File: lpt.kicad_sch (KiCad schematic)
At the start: 28 parts, among them J4 DB25 FEMALE, K1 OJS-SH-124HMF, Q4 BC847, Q5 BC857, U3 LM358, U4 74HC245, U5 74HC245, U6 ACSL-6310, U7 ACSL-6310

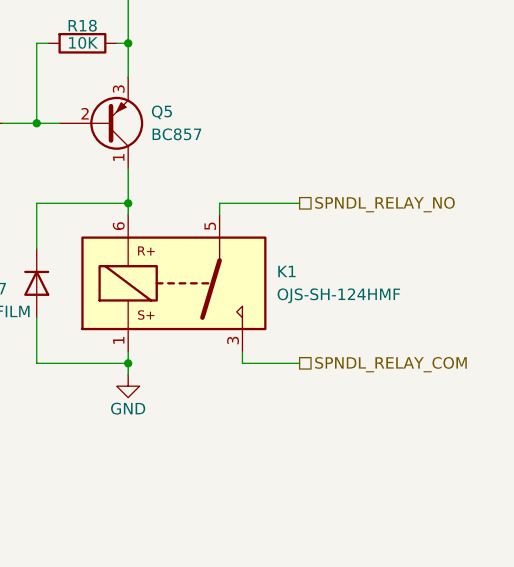
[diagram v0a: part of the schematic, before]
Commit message: Change and reposition JP16/17 connector to screw terminal.
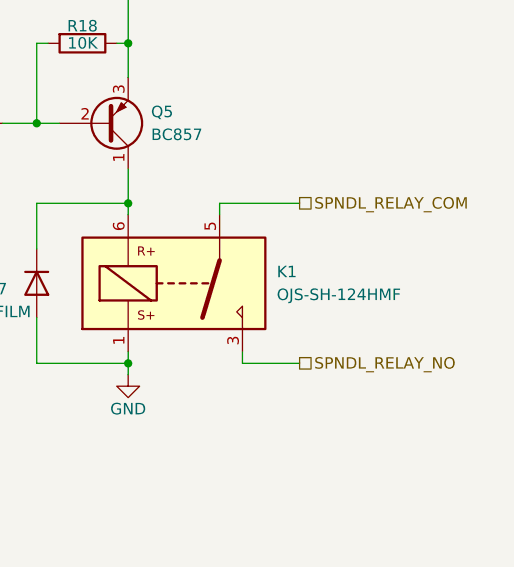
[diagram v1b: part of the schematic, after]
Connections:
- net SPNDL_RELAY_COM: now also K1.5; no longer K1.3
- net SPNDL_RELAY_NO: now also K1.3; no longer K1.5
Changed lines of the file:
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@@
     (effects (font (size 1.27 1.27)) (justify left))
   )
-  (hierarchical_label "SPNDL_RELAY_COM" (shape passive) (at 261.62 157.48 0)
+  (hierarchical_label "SPNDL_RELAY_COM" (shape passive) (at 261.62 139.7 0)
     (effects (font (size 1.27 1.27)) (justify left))
   )
@@
     (effects (font (size 1.27 1.27)) (justify left))
   )
-  (hierarchical_label "SPNDL_RELAY_NO" (shape passive) (at 261.62 139.7 0)
+  (hierarchical_label "SPNDL_RELAY_NO" (shape passive) (at 261.62 157.48 0)
     (effects (font (size 1.27 1.27)) (justify left))
   )
@@
       (effects (font (size 1.27 1.27)) hide)
     )
+    (pin "1")
+    (pin "2")
+    (pin "3")
     (pin "5")
     (pin "6")
     (pin "7")
+    (pin "4")
+    (pin "8")
   )
   (symbol (lib_id "Device:R_Pack04") (at 161.29 82.55 0) (mirror x) (unit 1)
@@
       (effects (font (size 1.27 1.27)) hide)
     )
+    (pin "1")
+    (pin "2")
+    (pin "3")
+    (pin "5")
+    (pin "6")
+    (pin "7")
     (pin "4")
     (pin "8")
@@
     (pin "2")
     (pin "3")
+    (pin "5")
+    (pin "6")
+    (pin "7")
+    (pin "4")
+    (pin "8")
   )
   (symbol (lib_id "Connector:DB25_Female_MountingHoles") (at 31.75 68.58 0) (mirror y) (unit 1)

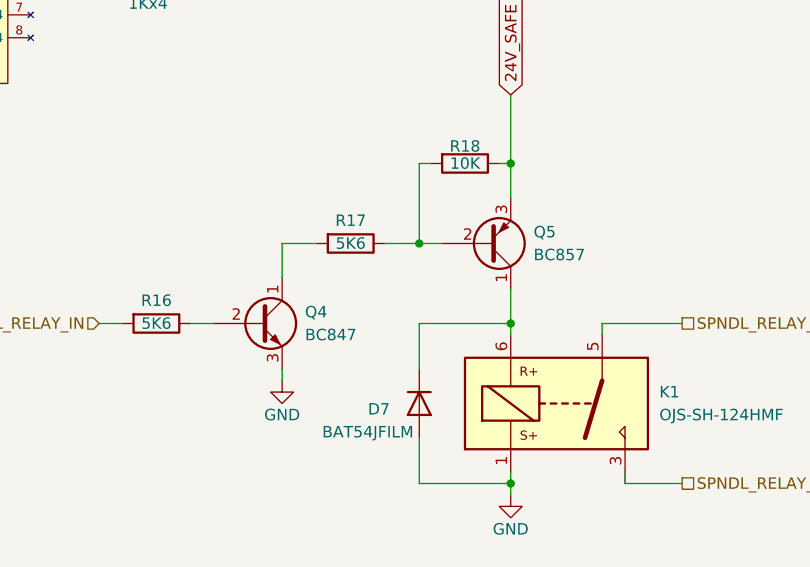
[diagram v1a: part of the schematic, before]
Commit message: Correct Q5 pin muddle.
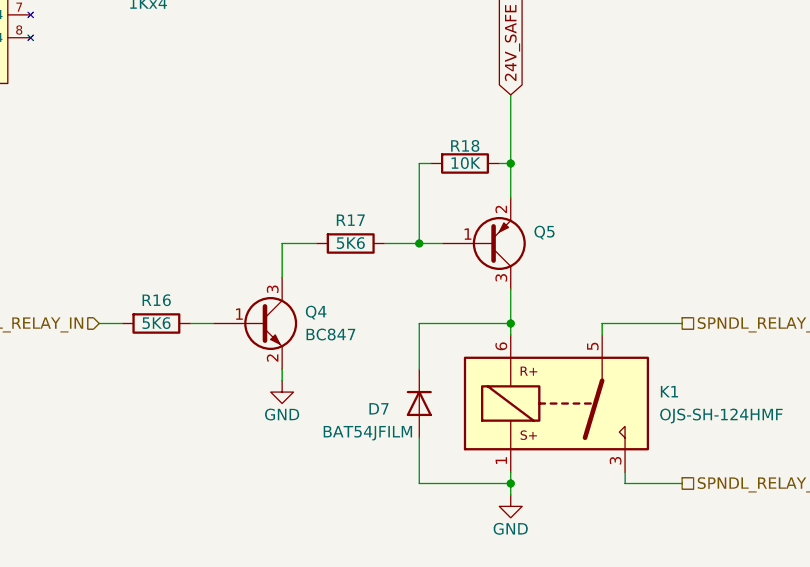
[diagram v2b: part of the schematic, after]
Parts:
- Q4: footprint -Project:SOT-23_DOT -> Package_TO_SOT_SMD:SOT-23; symbol Transistor_BJT:BC547 -> Transistor_BJT:BC847
- Q5: value BC857 -> (none); footprint -Project:SOT-23_DOT -> (none); symbol Device:Q_PNP_CBE -> Device:Q_PNP_BEC
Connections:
- net 24V_SAFE: now also Q5.2 (E); no longer Q5.3 (E)
- net GND: now also Q4.2 (E); no longer Q4.3 (E)
- net at D7.1 (K), K1.6: now also Q5.3 (C); no longer Q5.1 (C)
- net at R17.1, R18.2: now also Q5.1 (B); no longer Q5.2 (B)
- net at R16.1: now also Q4.1 (B); no longer Q4.2 (B)
- net at R17.2: now also Q4.3 (C); no longer Q4.1 (C)
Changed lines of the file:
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@@
     (pin "1")
   )
-  (symbol (lib_id "Device:Q_PNP_CBE") (at 240.03 130.81 0) (mirror x) (unit 1)
+  (symbol (lib_id "Device:Q_PNP_BEC") (at 240.03 130.81 0) (mirror x) (unit 1)
     (in_bom yes) (on_board yes) (fields_autoplaced)
     (property "Reference" "Q5" (id 0) (at 245.11 129.5399 0)
       (effects (font (size 1.27 1.27)) (justify left))
     )
-    (property "Value" "BC857" (id 1) (at 245.11 132.0799 0)
-      (effects (font (size 1.27 1.27)) (justify left))
-    )
-    (property "Footprint" "-Project:SOT-23_DOT" (id 2) (at 245.11 133.35 0)
+    (property "Value" "" (id 1) (at 245.11 132.0799 0)
+      (effects (font (size 1.27 1.27)) (justify left))
+    )
+    (property "Footprint" "" (id 2) (at 245.11 133.35 0)
       (effects (font (size 1.27 1.27)) hide)
     )
@@
     (pin "1")
   )
-  (symbol (lib_id "Transistor_BJT:BC547") (at 214.63 139.7 0) (unit 1)
+  (symbol (lib_id "Transistor_BJT:BC847") (at 214.63 139.7 0) (unit 1)
     (in_bom yes) (on_board yes)
     (property "Reference" "Q4" (id 0) (at 219.71 138.43 0)
@@
       (effects (font (size 1.27 1.27)) (justify left))
     )
-    (property "Footprint" "-Project:SOT-23_DOT" (id 2) (at 219.71 141.605 0)
+    (property "Footprint" "Package_TO_SOT_SMD:SOT-23" (id 2) (at 219.71 141.605 0)
       (effects (font (size 1.27 1.27) italic) (justify left) hide)
     )
-    (property "Datasheet" "https://www.onsemi.com/pub/Collateral/BC550-D.pdf" (id 3) (at 214.63 139.7 0)
+    (property "Datasheet" "http://www.infineon.com/dgdl/Infineon-BC847SERIES_BC848SERIES_BC849SERIES_BC850SERIES-DS-v01_01-en.pdf?fileId=db3a304314dca389011541d4630a1657" (id 3) (at 214.63 139.7 0)
       (effects (font (size 1.27 1.27)) (justify left) hide)
     )

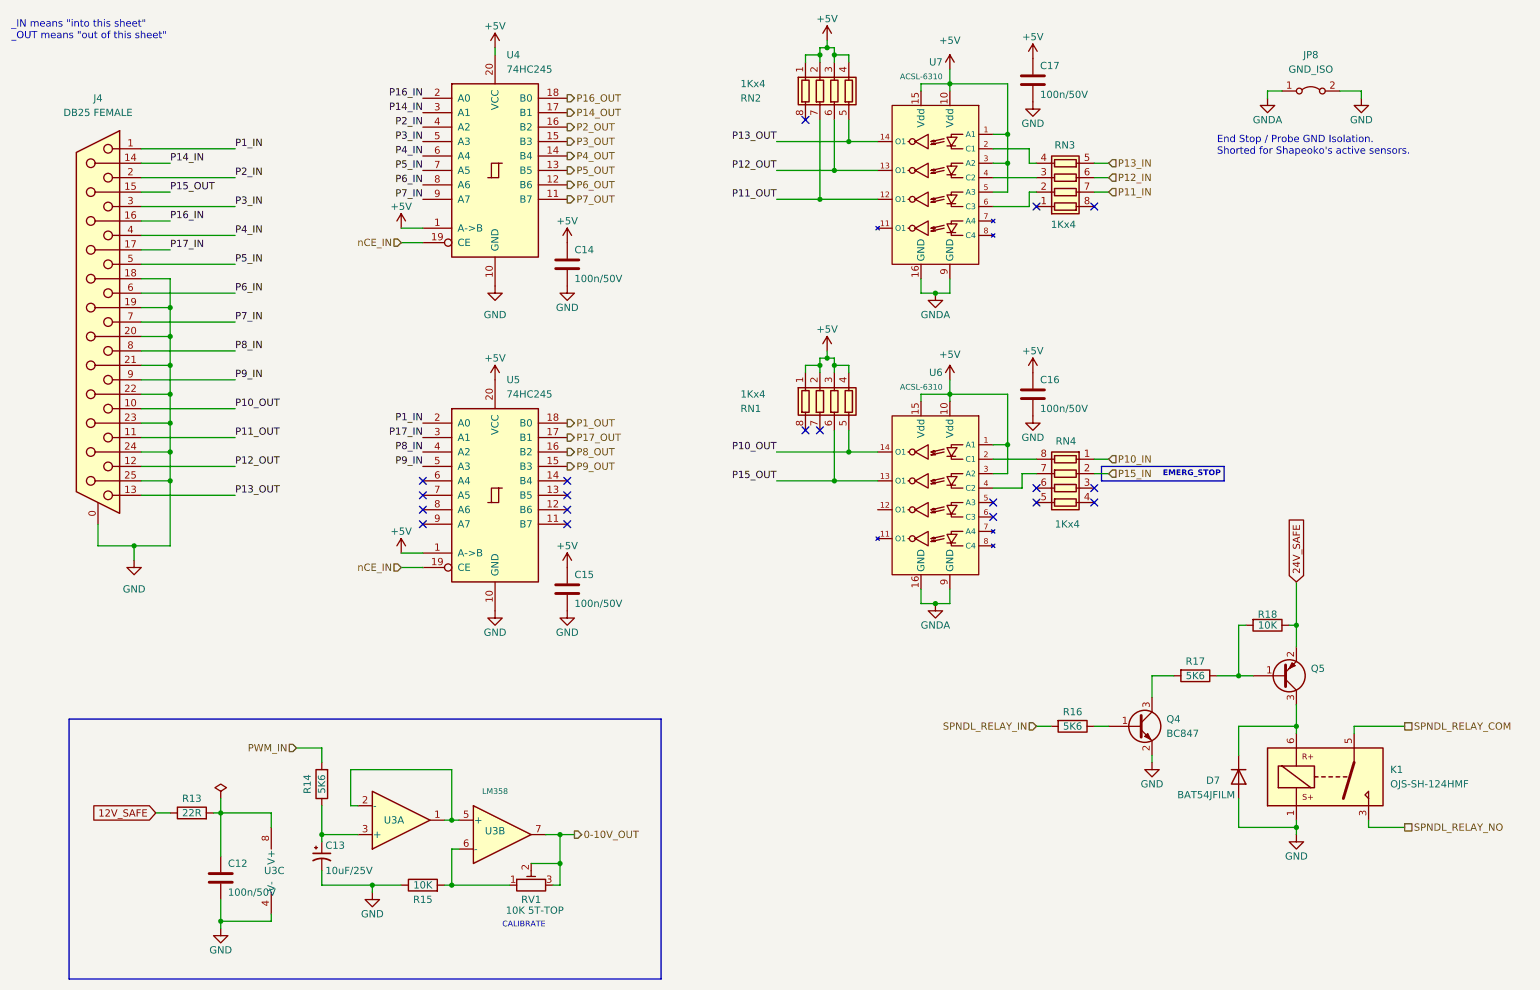
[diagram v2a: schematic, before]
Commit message: Charge pump signal re-routed.
Funny how the CP signal can't get through if /CE not asserted but /CE can only be asserted if the charge pump signal present. Oops. :/
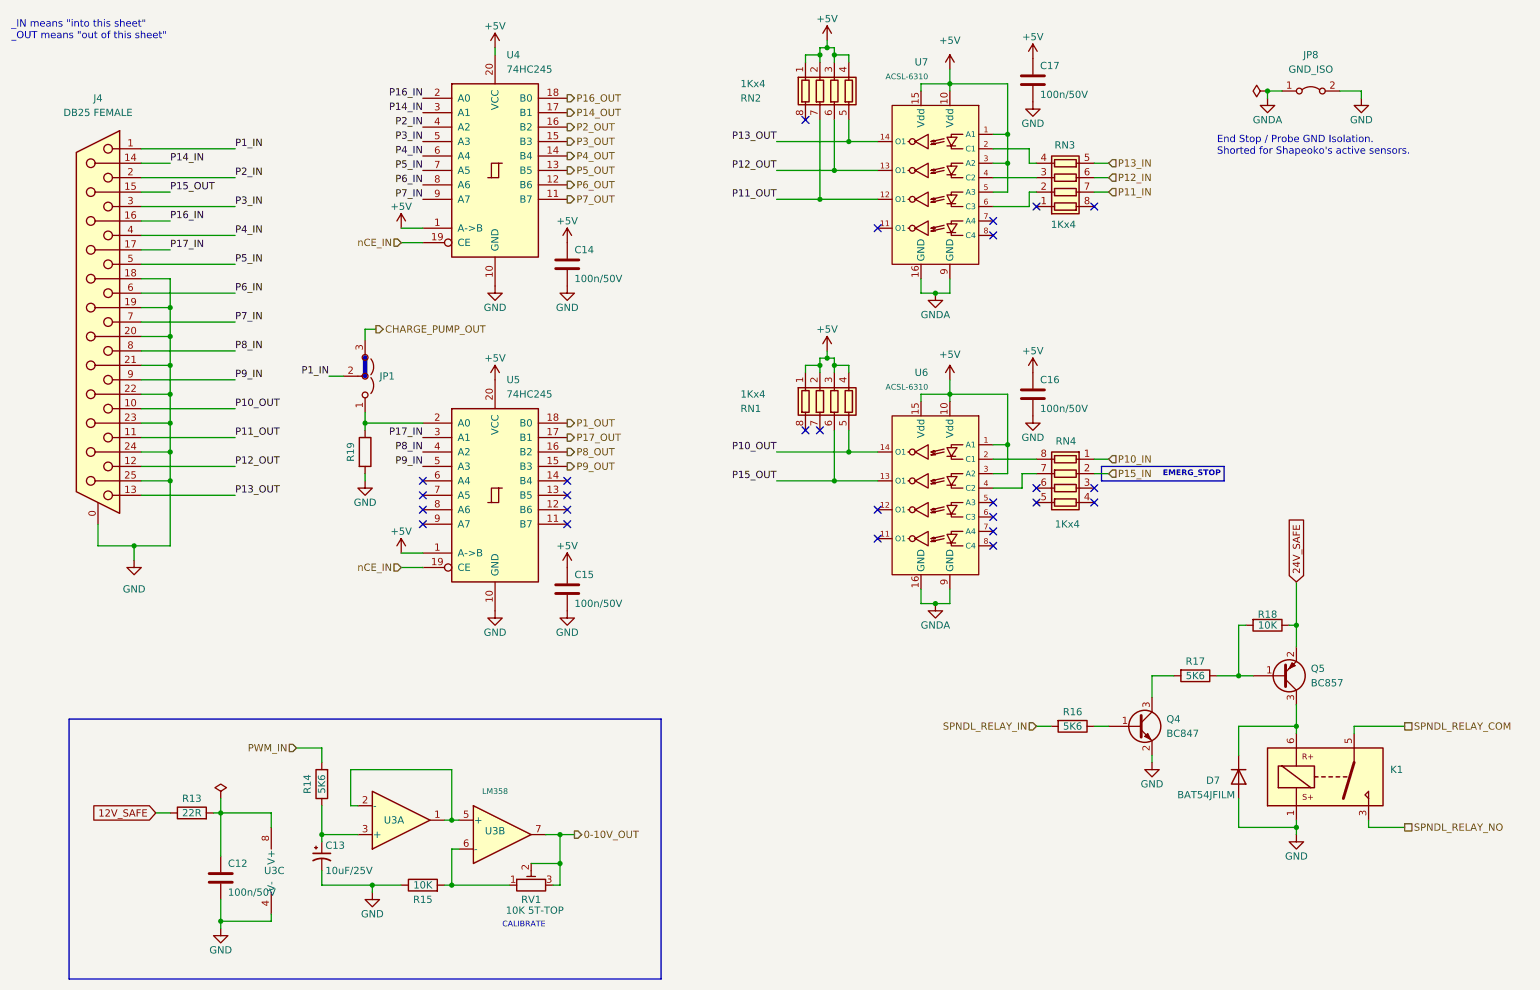
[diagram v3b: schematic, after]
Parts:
- added JP1: 1x03_2.54, Connector_PinHeader_2.54mm:PinHeader_1x03_P2.54mm_Vertical, symbol Jumper:Jumper_3_Open
- added R19: (no value), Resistor_SMD:R_0603_1608Metric, symbol Device:R
- K1: value OJS-SH-124HMF -> (none)
- Q5: value (none) -> BC857; footprint (none) -> -Project:SOT-23_DOT
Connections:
- net GND: now also R19.2
- net P1_IN: now also JP1.2 (C); no longer U5.2 (A0)
- new net: JP1.1 (A), R19.1, U5.2 (A0)
- new net CHARGE_PUMP_OUT: JP1.3 (B)
- no-connect marks 19 -> 26

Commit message: Corrected J2 pinout
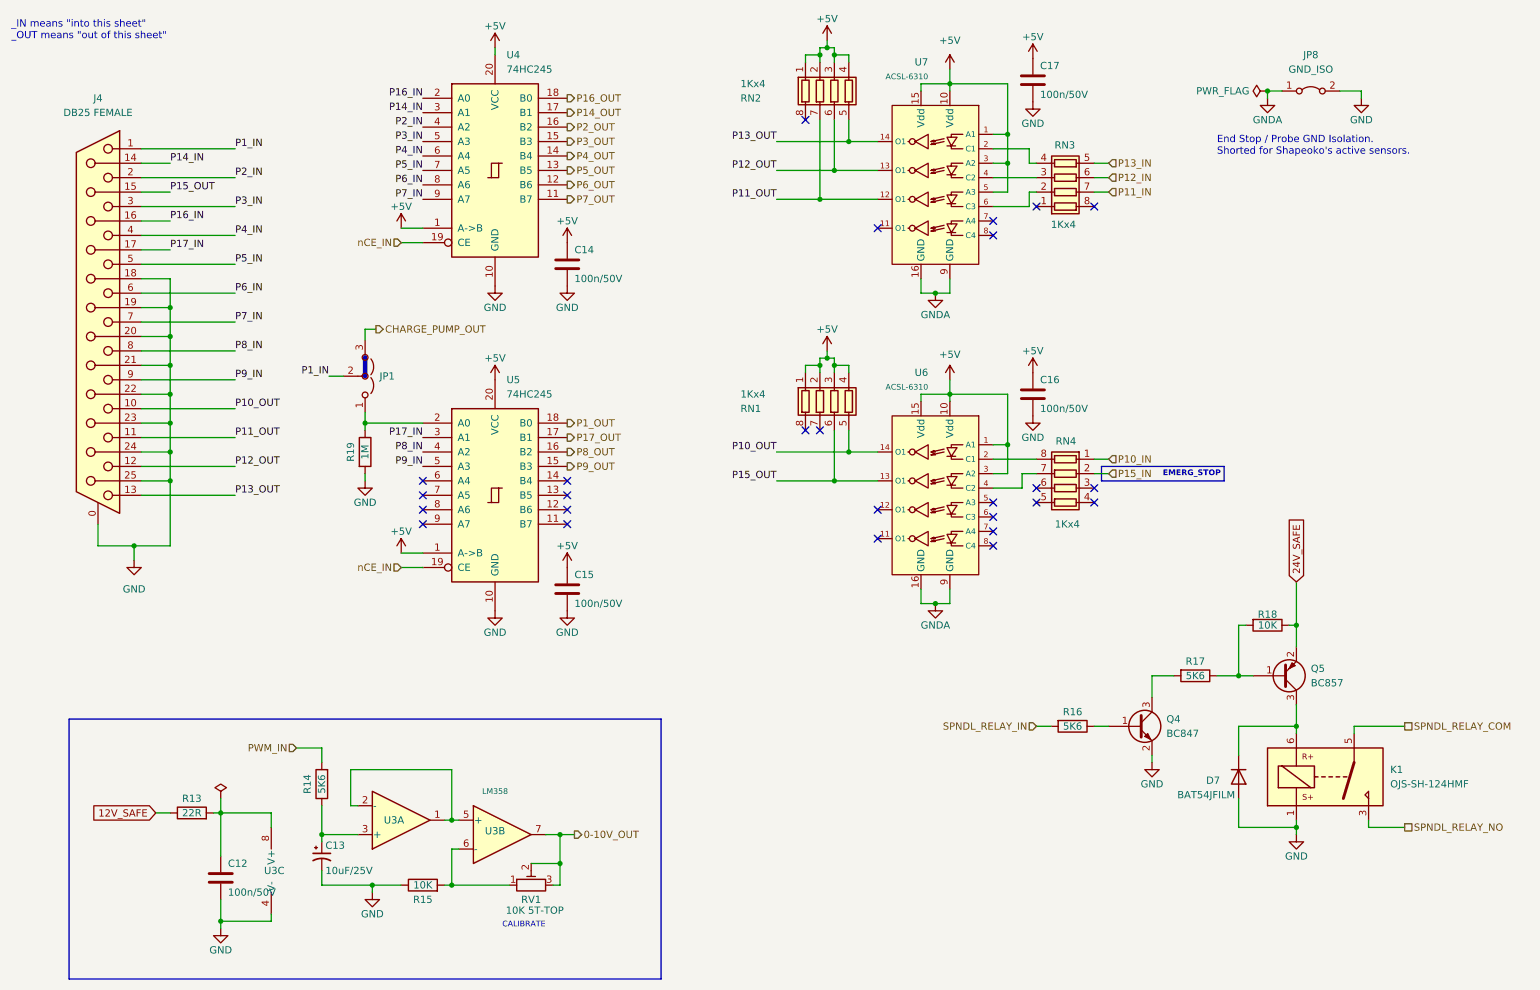
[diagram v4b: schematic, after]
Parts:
- K1: value (none) -> OJS-SH-124HMF
- R19: value (none) -> 1M
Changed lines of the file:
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@@
       (effects (font (size 1.27 1.27)) hide)
     )
-    (property "Value" "" (id 1) (at 234.315 27.9399 90)
+    (property "Value" "PWR_FLAG" (id 1) (at 234.315 27.9399 90)
       (effects (font (size 1.27 1.27)) (justify left))
     )
@@
     (in_bom yes) (on_board yes)
     (property "Reference" "R19" (id 0) (at 76.2 91.44 90))
-    (property "Value" "" (id 1) (at 78.74 91.44 90))
+    (property "Value" "1M" (id 1) (at 78.74 91.44 90))
     (property "Footprint" "Resistor_SMD:R_0603_1608Metric" (id 2) (at 76.962 91.44 90)
       (effects (font (size 1.27 1.27)) hide)
@@
       (effects (font (size 1.27 1.27)) (justify left))
     )
-    (property "Value" "" (id 1) (at 259.08 149.86 0)
-      (effects (font (size 1.27 1.27)) (justify left))
-    )
+    (property "Value" "OJS-SH-124HMF" (id 1) (at 259.08 149.86 0)
+      (effects (font (size 1.27 1.27)) (justify left))
+    )

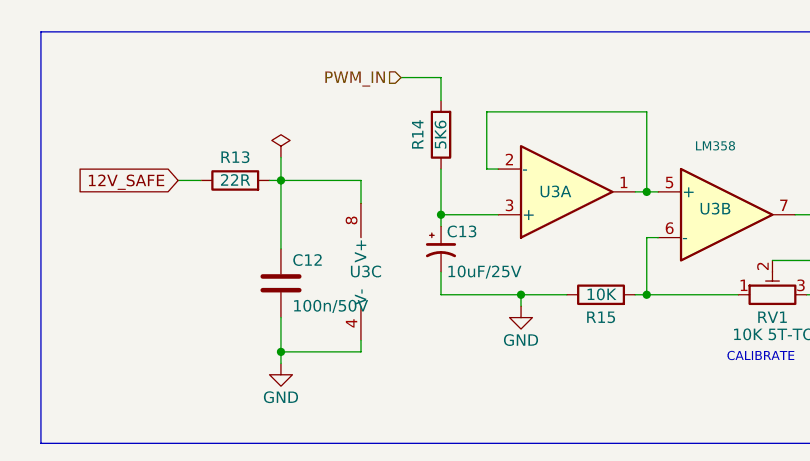
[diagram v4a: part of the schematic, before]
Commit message: Fixed all three endstop pinout errors. :/
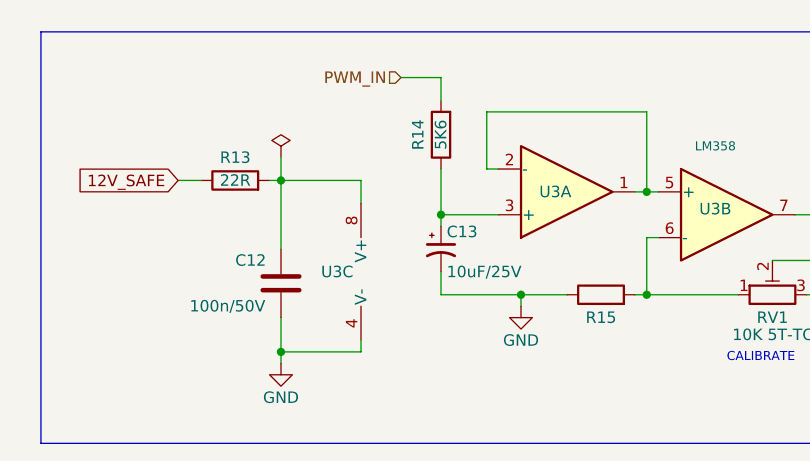
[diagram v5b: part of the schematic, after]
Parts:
- R15: value 10K -> (none)
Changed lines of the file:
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@@
     (in_bom yes) (on_board yes)
     (property "Reference" "R15" (id 0) (at 88.9 170.18 90))
-    (property "Value" "10K" (id 1) (at 88.9 167.64 90))
+    (property "Value" "" (id 1) (at 88.9 167.64 90))
     (property "Footprint" "Resistor_SMD:R_0603_1608Metric" (id 2) (at 88.9 169.418 90)
       (effects (font (size 1.27 1.27)) hide)
@@
   (symbol (lib_id "Device:C") (at 53.34 166.37 0) (unit 1)
     (in_bom yes) (on_board yes)
-    (property "Reference" "C12" (id 0) (at 54.61 163.83 0)
-      (effects (font (size 1.27 1.27)) (justify left))
-    )
-    (property "Value" "100n/50V" (id 1) (at 54.61 168.91 0)
+    (property "Reference" "C12" (id 0) (at 48.26 163.83 0)
+      (effects (font (size 1.27 1.27)) (justify left))
+    )
+    (property "Value" "100n/50V" (id 1) (at 43.18 168.91 0)
       (effects (font (size 1.27 1.27)) (justify left))
     )
@@
   (symbol (lib_id "Amplifier_Operational:LM358") (at 64.77 165.1 0) (unit 3)
     (in_bom yes) (on_board yes)
-    (property "Reference" "U3" (id 0) (at 60.96 165.1 0)
-      (effects (font (size 1.27 1.27)) (justify left))
-    )
+    (property "Reference" "U3" (id 0) (at 57.785 165.1 0)
+      (effects (font (size 1.27 1.27)) (justify left))
+    )

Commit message: JLCPCB_V3.0
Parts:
- R15: value (none) -> 5K1
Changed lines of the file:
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@@
   (title_block
     (title "Shapeoko LPT Interface — LPT Interface")
-    (date "2022-06-02")
-    (rev "2.0")
+    (date "2022-07-09")
+    (rev "3.0")
   )
   (junction (at 113.03 158.75) (diameter 0) (color 0 0 0 0)
@@
     (in_bom yes) (on_board yes)
     (property "Reference" "R15" (id 0) (at 88.9 170.18 90))
-    (property "Value" "" (id 1) (at 88.9 167.64 90))
+    (property "Value" "5K1" (id 1) (at 88.9 167.64 90))
     (property "Footprint" "Resistor_SMD:R_0603_1608Metric" (id 2) (at 88.9 169.418 90)
       (effects (font (size 1.27 1.27)) hide)

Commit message: Two board version taking shape
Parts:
- removed C12: 100n/50V, Capacitor_SMD:C_0603_1608Metric, symbol Device:C
- removed C13: 10uF/25V, Capacitor_SMD:C_0603_1608Metric, symbol Device:C_Polarized_Small_US
- removed D7: BAT54JFILM, -Project:D_SOD-323_DOT, symbol Device:D
- removed K1: OJS-SH-124HMF, -Project:Relay_SPST_OJS_24V_10A, symbol 3rd-party:RELAY_TE_OJS_24V_10A
- removed Q4: BC847, Package_TO_SOT_SMD:SOT-23, symbol Transistor_BJT:BC847
- removed Q5: BC857, -Project:SOT-23_DOT, symbol Device:Q_PNP_BEC
- removed R13: 22R, Resistor_SMD:R_0603_1608Metric, symbol Device:R
- removed R14, R16, R17: 5K6, Resistor_SMD:R_0603_1608Metric, symbol Device:R
- removed R15: 5K1, Resistor_SMD:R_0603_1608Metric, symbol Device:R
- removed R18: 10K, Resistor_SMD:R_0603_1608Metric, symbol Device:R
- removed RV1: 10K 5T-TOP, Potentiometer_SMD:Potentiometer_Bourns_3314J_Vertical, symbol Device:R_Potentiometer_Trim
- removed U3: LM358, Package_SO:SOIC-8_3.9x4.9mm_P1.27mm, symbol Amplifier_Operational:LM358
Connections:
- net P11_OUT: now also RN2.8 (R1.2); no longer RN2.7 (R2.2)
- net P12_OUT: now also RN2.7 (R2.2); no longer RN2.6 (R3.2)
- net P15_IN renamed EMERG_STOP_IN
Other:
- note removed: "CALIBRATE"
- note removed: "EMERG_STOP"
- moved on the sheet: C16
